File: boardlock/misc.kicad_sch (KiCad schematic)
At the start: 13 parts

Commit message: more Zecong edits
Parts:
- added H? (x4): MountingHole, symbol Mechanical:MountingHole
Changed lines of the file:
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@@
+    )
+  )
+  (symbol (lib_id "Mechanical:MountingHole") (at 59.69 147.32 0) (unit 1)
+    (in_bom yes) (on_board yes) (dnp no) (fields_autoplaced)
+    (property "Reference" "H?" (at 62.23 146.05 0)
+      (effects (font (size 1.27 1.27)) (justify left))
+    )
+    (property "Value" "MountingHole" (at 62.23 148.59 0)
+      (effects (font (size 1.27 1.27)) (justify left))
+    )
+    (property "Footprint" "" (at 59.69 147.32 0)
+      (effects (font (size 1.27 1.27)) hide)
+    )
+    (property "Datasheet" "~" (at 59.69 147.32 0)
+      (effects (font (size 1.27 1.27)) hide)
+    )
+    (instances
+      (project "boardlock"
+        (path "/e1fc29ce-837e-4062-84d8-c7e423f9eab9/ace912f2-c3e9-4bf3-99ba-49d1d353f0f6"
+          (reference "H?") (unit 1)
+        )
+      )
     )
   )
@@
     )
   )
+  (symbol (lib_id "Mechanical:MountingHole") (at 34.29 137.16 0) (unit 1)
+    (in_bom yes) (on_board yes) (dnp no) (fields_autoplaced)
+    (property "Reference" "H?" (at 36.83 135.89 0)
+      (effects (font (size 1.27 1.27)) (justify left))
+    )
+    (property "Value" "MountingHole" (at 36.83 138.43 0)
+      (effects (font (size 1.27 1.27)) (justify left))
+    )
+    (property "Footprint" "" (at 34.29 137.16 0)
+      (effects (font (size 1.27 1.27)) hide)
+    )
+    (property "Datasheet" "~" (at 34.29 137.16 0)
+      (effects (font (size 1.27 1.27)) hide)
+    )
+    (instances
+      (project "boardlock"
+        (path "/e1fc29ce-837e-4062-84d8-c7e423f9eab9/ace912f2-c3e9-4bf3-99ba-49d1d353f0f6"
+          (reference "H?") (unit 1)
+        )
+      )
+    )
+  )
   (symbol (lib_id "Connector:TestPoint") (at 165.1 26.67 270) (unit 1)
     (in_bom yes) (on_board yes) (dnp no)
@@
     )
   )
+  (symbol (lib_id "Mechanical:MountingHole") (at 34.29 147.32 0) (unit 1)
+    (in_bom yes) (on_board yes) (dnp no) (fields_autoplaced)
+    (property "Reference" "H?" (at 36.83 146.05 0)
+      (effects (font (size 1.27 1.27)) (justify left))
+    )
+    (property "Value" "MountingHole" (at 36.83 148.59 0)
+      (effects (font (size 1.27 1.27)) (justify left))
+    )
+    (property "Footprint" "" (at 34.29 147.32 0)
+      (effects (font (size 1.27 1.27)) hide)
+    )
+    (property "Datasheet" "~" (at 34.29 147.32 0)
+      (effects (font (size 1.27 1.27)) hide)
+    )
+    (instances
+      (project "boardlock"
+        (path "/e1fc29ce-837e-4062-84d8-c7e423f9eab9/ace912f2-c3e9-4bf3-99ba-49d1d353f0f6"
+          (reference "H?") (unit 1)
+        )
+      )
+    )
+  )
   (symbol (lib_id "Connector:TestPoint") (at 31.75 22.86 270) (unit 1)
     (in_bom yes) (on_board yes) (dnp no)
@@
         )
       )
+    )
+  )
+  (symbol (lib_id "Mechanical:MountingHole") (at 59.69 137.16 0) (unit 1)
+    (in_bom yes) (on_board yes) (dnp no) (fields_autoplaced)
+    (property "Reference" "H?" (at 62.23 135.89 0)
+      (effects (font (size 1.27 1.27)) (justify left))
+    )
+    (property "Value" "MountingHole" (at 62.23 138.43 0)
+      (effects (font (size 1.27 1.27)) (justify left))
+    )
+    (property "Footprint" "" (at 59.69 137.16 0)
+      (effects (font (size 1.27 1.27)) hide)
+    )
+    (property "Datasheet" "~" (at 59.69 137.16 0)
+      (effects (font (size 1.27 1.27)) hide)
+    )
+    (instances
+      (project "boardlock"
+        (path "/e1fc29ce-837e-4062-84d8-c7e423f9eab9/ace912f2-c3e9-4bf3-99ba-49d1d353f0f6"
+          (reference "H?") (unit 1)
+        )
+      )

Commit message: buttons and stuff
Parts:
- added C25: C_Small, symbol Device:C_Small
- added TP15: BUTTON_EXT, symbol Connector:TestPoint
- added TP15: GPS_POWER, symbol Connector:TestPoint
- added TP15: RGB_B, symbol Connector:TestPoint
- added TP16: RGB_R, symbol Connector:TestPoint
- added TP16: IMU_POWER, symbol Connector:TestPoint
- added TP16: RST_N, symbol Connector:TestPoint
- added TP4: BUTTON_INT, symbol Connector:TestPoint
- added TP4: GPS_EXTINT, symbol Connector:TestPoint
- added TP9: BOOT, symbol Connector:TestPoint
- added TP9: IMU_INT2, symbol Connector:TestPoint
- added TP9: RGB_G, symbol Connector:TestPoint
- added U9: MAX7375, Package_TO_SOT_SMD:SOT-323_SC-70, symbol Oscillator:MAX7375AXR105
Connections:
- new net +3V3: C25.2, U9.1 (V+)
- new net GND: C25.1, U9.3 (GND)
- new net M_BOOT: TP9.1
- new net M_BUTTON_EXT: TP15.1
- new net M_BUTTON_INT: TP4.1
- new net M_CLK_EXT: U9.2 (CLOCK)
- new net M_GPS_EXTINT: TP4.1
- new net M_GPS_POWER: TP15.1
- new net M_IMU_INT2: TP9.1
- new net M_IMU_POWER: TP16.1
- new net M_RGB_B: TP15.1
- new net M_RGB_G: TP9.1
- new net M_RGB_R: TP16.1
- new net M_RST_N: TP16.1
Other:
- note added: "Buttons"
- note added: "RGB"
- note added: "Sensors"
- note added: "uC dev kit doesn't use external clk so we may not need this"

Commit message: lab updates
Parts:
- removed C25: C_Small, symbol Device:C_Small
- removed U9: MAX7375, Package_TO_SOT_SMD:SOT-323_SC-70, symbol Oscillator:MAX7375AXR105
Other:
- note added: "add 1 per global label into uC"
- note removed: "uC dev kit doesn't use external clk so we may not need this"
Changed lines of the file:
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@@
     (company "Schetmatic")
   )
-  (junction (at 119.38 99.06) (diameter 0) (color 0 0 0 0)
-  )
   (wire (pts (xy 74.93 26.67) (xy 73.66 26.67))
     (stroke (width 0) (type default))
@@
     (stroke (width 0) (type default))
   )
-  (wire (pts (xy 119.38 96.52) (xy 119.38 99.06))
-    (stroke (width 0) (type default))
-  )
   (wire (pts (xy 210.82 30.48) (xy 212.09 30.48))
     (stroke (width 0) (type default))
   )
-  (wire (pts (xy 106.68 99.06) (xy 109.22 99.06))
-    (stroke (width 0) (type default))
-  )
-  (wire (pts (xy 106.68 99.06) (xy 106.68 101.6))
-    (stroke (width 0) (type default))
-  )
   (wire (pts (xy 163.83 26.67) (xy 165.1 26.67))
     (stroke (width 0) (type default))
@@
     (stroke (width 0) (type default))
   )
-  (wire (pts (xy 114.3 99.06) (xy 119.38 99.06))
-    (stroke (width 0) (type default))
-  )
   (wire (pts (xy 30.48 53.34) (xy 31.75 53.34))
     (stroke (width 0) (type default))
@@
     (stroke (width 0) (type default))
   )
-  (wire (pts (xy 119.38 99.06) (xy 119.38 101.6))
-    (stroke (width 0) (type default))
-  )
   (wire (pts (xy 118.11 57.15) (xy 119.38 57.15))
     (stroke (width 0) (type default))
@@
     (stroke (width 0) (type default))
   )
-  (wire (pts (xy 119.38 116.84) (xy 119.38 119.38))
-    (stroke (width 0) (type default))
-  )
-  (wire (pts (xy 129.54 109.22) (xy 132.08 109.22))
-    (stroke (width 0) (type default))
-  )
   (wire (pts (xy 210.82 26.67) (xy 212.09 26.67))
     (stroke (width 0) (type default))
@@
     (effects (font (size 1.27 1.27) (thickness 0.254) bold) (justify left bottom))
   )
-  (text "uC dev kit doesn't use external clk so we may not need this"
-    (at 95.25 128.27 0)
-    (effects (font (size 1.27 1.27)) (justify left bottom))
+  (text "add 1 per global label into uC\n" (at 184.15 55.88 0)
+    (effects (font (size 1.27 1.27) bold) (justify left bottom))
   )
   (text "UART\n" (at 78.74 20.32 0)
@@
     (property "Intersheetrefs" "${INTERSHEET_REFS}" (at 62.2686 60.96 0)
       (effects (font (size 1.27 1.27)) (justify right) hide)
-    )
-  )
-  (global_label "M_CLK_EXT" (shape output) (at 132.08 109.22 0) (fields_autoplaced)
-    (effects (font (size 1.27 1.27)) (justify left))
-    (property "Intersheetrefs" "${INTERSHEET_REFS}" (at 145.346 109.22 0)
-      (effects (font (size 1.27 1.27)) (justify left) hide)
-    )
-  )
-  (symbol (lib_id "power:GND") (at 106.68 101.6 0) (unit 1)
-    (in_bom yes) (on_board yes) (dnp no) (fields_autoplaced)
-    (property "Reference" "#PWR077" (at 106.68 107.95 0)
-      (effects (font (size 1.27 1.27)) hide)
-    )
-    (property "Value" "GND" (at 106.68 106.68 0)
-      (effects (font (size 1.27 1.27)))
-    )
-    (property "Footprint" "" (at 106.68 101.6 0)
-      (effects (font (size 1.27 1.27)) hide)
-    )
-    (property "Datasheet" "" (at 106.68 101.6 0)
-      (effects (font (size 1.27 1.27)) hide)
-    )
-    (pin "1")
-    (instances
-      (project "boardlock"
-        (path "/e1fc29ce-837e-4062-84d8-c7e423f9eab9/ace912f2-c3e9-4bf3-99ba-49d1d353f0f6"
-          (reference "#PWR077") (unit 1)
-        )
-      )
     )
   )
@@
     )
   )
-  (symbol (lib_id "power:GND") (at 119.38 119.38 0) (unit 1)
-    (in_bom yes) (on_board yes) (dnp no) (fields_autoplaced)
-    (property "Reference" "#PWR075" (at 119.38 125.73 0)
-      (effects (font (size 1.27 1.27)) hide)
-    )
-    (property "Value" "GND" (at 119.38 124.46 0)
-      (effects (font (size 1.27 1.27)))
-    )
-    (property "Footprint" "" (at 119.38 119.38 0)
-      (effects (font (size 1.27 1.27)) hide)
-    )
-    (property "Datasheet" "" (at 119.38 119.38 0)
-      (effects (font (size 1.27 1.27)) hide)
-    )
-    (pin "1")
-    (instances
-      (project "boardlock"
-        (path "/e1fc29ce-837e-4062-84d8-c7e423f9eab9/ace912f2-c3e9-4bf3-99ba-49d1d353f0f6"
-          (reference "#PWR075") (unit 1)
-        )
-      )
-    )
-  )
   (symbol (lib_id "Connector:TestPoint") (at 31.75 26.67 270) (unit 1)
     (in_bom yes) (on_board yes) (dnp no)
@@
     )
   )
-  (symbol (lib_id "Oscillator:MAX7375AXR105") (at 119.38 109.22 0) (unit 1)
-    (in_bom yes) (on_board yes) (dnp no) (fields_autoplaced)
-    (property "Reference" "U9" (at 113.03 107.95 0)
-      (effects (font (size 1.27 1.27)) (justify right))
-    )
-    (property "Value" "MAX7375" (at 113.03 110.49 0)
-      (effects (font (size 1.27 1.27)) (justify right))
-    )
-    (property "Footprint" "Package_TO_SOT_SMD:SOT-323_SC-70" (at 147.32 118.11 0)
-      (effects (font (size 1.27 1.27)) hide)
-    )
-    (property "Datasheet" "https://datasheets.maximintegrated.com/en/ds/MAX7375.pdf" (at 116.84 109.22 0)
-      (effects (font (size 1.27 1.27)) hide)
-    )
-    (pin "1")
-    (pin "2")
-    (pin "3")
-    (instances
-      (project "boardlock"
-        (path "/e1fc29ce-837e-4062-84d8-c7e423f9eab9/ace912f2-c3e9-4bf3-99ba-49d1d353f0f6"
-          (reference "U9") (unit 1)
-        )
-      )
-    )
-  )
   (symbol (lib_id "Connector:TestPoint") (at 31.75 57.15 270) (unit 1)
     (in_bom yes) (on_board yes) (dnp no)
@@
         (path "/e1fc29ce-837e-4062-84d8-c7e423f9eab9/ace912f2-c3e9-4bf3-99ba-49d1d353f0f6"
           (reference "TP20") (unit 1)
-        )
-      )
-    )
-  )
-  (symbol (lib_id "Device:C_Small") (at 111.76 99.06 90) (unit 1)
-    (in_bom yes) (on_board yes) (dnp no) (fields_autoplaced)
-    (property "Reference" "C25" (at 111.7663 92.71 90)
-      (effects (font (size 1.27 1.27)))
-    )
-    (property "Value" "C_Small" (at 111.7663 95.25 90)
-      (effects (font (size 1.27 1.27)))
-    )
-    (property "Footprint" "" (at 111.76 99.06 0)
-      (effects (font (size 1.27 1.27)) hide)
-    )
-    (property "Datasheet" "~" (at 111.76 99.06 0)
-      (effects (font (size 1.27 1.27)) hide)
-    )
-    (pin "1")
-    (pin "2")
-    (instances
-      (project "boardlock"
-        (path "/e1fc29ce-837e-4062-84d8-c7e423f9eab9/ace912f2-c3e9-4bf3-99ba-49d1d353f0f6"
-          (reference "C25") (unit 1)
         )
       )
@@
         )
       )
-    )
-  )
-  (symbol (lib_id "power:+3V3") (at 119.38 96.52 0) (unit 1)
-    (in_bom yes) (on_board yes) (dnp no) (fields_autoplaced)
-    (property "Reference" "#PWR076" (at 119.38 100.33 0)
-      (effects (font (size 1.27 1.27)) hide)
-    )
-    (property "Value" "+3V3" (at 119.38 91.44 0)
-      (effects (font (size 1.27 1.27)))
-    )
-    (property "Footprint" "" (at 119.38 96.52 0)
-      (effects (font (size 1.27 1.27)) hide)
-    )
-    (property "Datasheet" "" (at 119.38 96.52 0)
-      (effects (font (size 1.27 1.27)) hide)
-    )
-    (pin "1")
-    (instances
-      (project "boardlock"
-        (path "/e1fc29ce-837e-4062-84d8-c7e423f9eab9/ace912f2-c3e9-4bf3-99ba-49d1d353f0f6"
-          (reference "#PWR076") (unit 1)
-        )
-      )

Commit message: not sure what I changed
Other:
- note added: "Audio"
- moved on the sheet: TP15, TP16, TP4, TP5, TP6, TP9

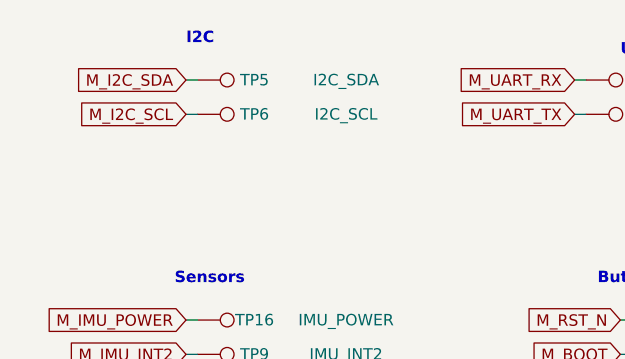
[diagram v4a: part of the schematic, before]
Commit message: added footprints and an LPF to audio
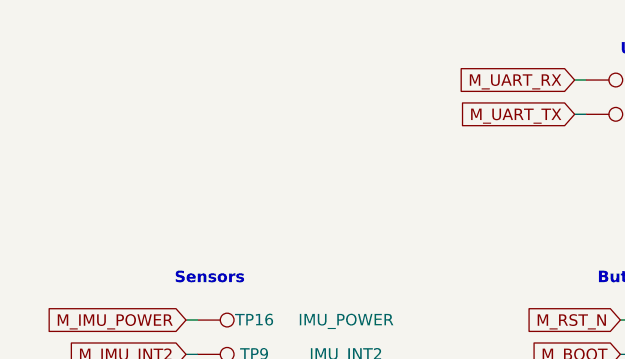
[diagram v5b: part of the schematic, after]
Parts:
- removed TP5: I2C_SDA, symbol Connector:TestPoint
- removed TP6: I2C_SCL, symbol Connector:TestPoint
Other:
- note removed: "I2C"
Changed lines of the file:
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@@
-    (stroke (width 0) (type default))
-  )
-  (wire (pts (xy 39.37 26.67) (xy 40.64 26.67))
     (stroke (width 0) (type default))
   )
@@
   )
   (wire (pts (xy 39.37 60.96) (xy 40.64 60.96))
-    (stroke (width 0) (type default))
-  )
-  (wire (pts (xy 39.37 22.86) (xy 40.64 22.86))
     (stroke (width 0) (type default))
   )
@@
     (effects (font (size 1.27 1.27) (thickness 0.254) bold) (justify left bottom))
   )
-  (text "I2C\n" (at 39.37 19.05 0)
-    (effects (font (size 1.27 1.27) (thickness 0.254) bold) (justify left bottom))
-  )
   (global_label "M_I2S_BCLK" (shape input) (at 124.46 30.48 180) (fields_autoplaced)
     (effects (font (size 1.27 1.27)) (justify right))
@@
     )
   )
-  (global_label "M_I2C_SCL" (shape input) (at 39.37 26.67 180) (fields_autoplaced)
-    (effects (font (size 1.27 1.27)) (justify right))
-    (property "Intersheetrefs" "${INTERSHEET_REFS}" (at 26.4063 26.67 0)
-      (effects (font (size 1.27 1.27)) (justify right) hide)
-    )
-  )
   (global_label "M_RGB_G" (shape input) (at 127 53.34 180) (fields_autoplaced)
     (effects (font (size 1.27 1.27)) (justify right))
@@
     (effects (font (size 1.27 1.27)) (justify right))
     (property "Intersheetrefs" "${INTERSHEET_REFS}" (at 159.6958 26.67 0)
-      (effects (font (size 1.27 1.27)) (justify right) hide)
-    )
-  )
-  (global_label "M_I2C_SDA" (shape input) (at 39.37 22.86 180) (fields_autoplaced)
-    (effects (font (size 1.27 1.27)) (justify right))
-    (property "Intersheetrefs" "${INTERSHEET_REFS}" (at 26.3458 22.86 0)
       (effects (font (size 1.27 1.27)) (justify right) hide)
     )
@@
     )
   )
-  (symbol (lib_id "Connector:TestPoint") (at 40.64 26.67 270) (unit 1)
-    (in_bom yes) (on_board yes) (dnp no)
-    (property "Reference" "TP6" (at 46.99 26.67 90)
-      (effects (font (size 1.27 1.27)))
-    )
-    (property "Value" "I2C_SCL" (at 57.15 26.67 90)
-      (effects (font (size 1.27 1.27)))
-    )
-    (property "Footprint" "" (at 40.64 31.75 0)
-      (effects (font (size 1.27 1.27)) hide)
-    )
-    (property "Datasheet" "~" (at 40.64 31.75 0)
-      (effects (font (size 1.27 1.27)) hide)
-    )
-    (pin "1")
-    (instances
-      (project "boardlock"
-        (path "/e1fc29ce-837e-4062-84d8-c7e423f9eab9/a4a6f965-a4d9-4da6-b64e-79eda0daabe5"
-          (reference "TP6") (unit 1)
-        )
-        (path "/e1fc29ce-837e-4062-84d8-c7e423f9eab9/ace912f2-c3e9-4bf3-99ba-49d1d353f0f6"
-          (reference "TP6") (unit 1)
-        )
-      )
-    )
-  )
   (symbol (lib_id "Mechanical:MountingHole") (at 34.29 137.16 0) (unit 1)
     (in_bom yes) (on_board yes) (dnp no) (fields_autoplaced)
@@
         )
       )
-    )
-  )
-  (symbol (lib_id "Connector:TestPoint") (at 40.64 22.86 270) (unit 1)
-    (in_bom yes) (on_board yes) (dnp no)
-    (property "Reference" "TP5" (at 46.99 22.86 90)
-      (effects (font (size 1.27 1.27)))
-    )
-    (property "Value" "I2C_SDA" (at 57.15 22.86 90)
-      (effects (font (size 1.27 1.27)))
-    )
-    (property "Footprint" "" (at 40.64 27.94 0)
-      (effects (font (size 1.27 1.27)) hide)
-    )
-    (property "Datasheet" "~" (at 40.64 27.94 0)
-      (effects (font (size 1.27 1.27)) hide)
-    )
-    (pin "1")
-    (instances
-      (project "boardlock"
-        (path "/e1fc29ce-837e-4062-84d8-c7e423f9eab9/a4a6f965-a4d9-4da6-b64e-79eda0daabe5"
-          (reference "TP5") (unit 1)
-        )
-        (path "/e1fc29ce-837e-4062-84d8-c7e423f9eab9/ace912f2-c3e9-4bf3-99ba-49d1d353f0f6"
-          (reference "TP5") (unit 1)
-        )
-      )
